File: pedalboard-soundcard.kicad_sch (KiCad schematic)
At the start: 21 parts, among them J1 RPi_GPIO, U1 AT24CS01-STUM, U2 NCP163, U3 NCP163, U5 NCP163

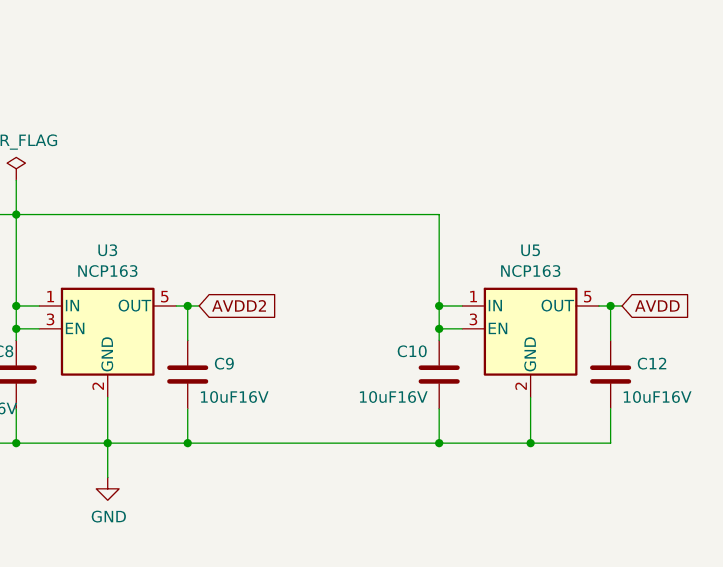
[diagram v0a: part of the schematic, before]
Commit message: Use Power Symbols for analog power
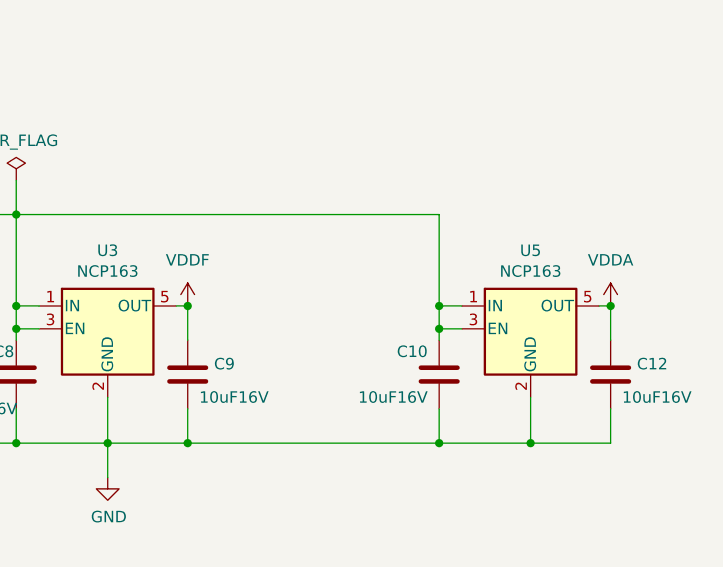
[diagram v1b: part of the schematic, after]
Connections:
- net AVDD renamed VDDA
- net AVDD2 renamed VDDF

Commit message: Add Fiducials and OSHW logo
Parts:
- added FID1, FID2, FID3, FID4: Fiducial, Fiducial:Fiducial_0.75mm_Mask1.5mm, symbol Mechanical:Fiducial
- added SYM1: Logo_Open_Hardware_Small, Symbol:OSHW-Logo2_9.8x8mm_SilkScreen, symbol Graphic:Logo_Open_Hardware_Small
- H1, H2, H3, H4: now left out of the parts list
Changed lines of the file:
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@@
   )
   (symbol (lib_id "Mechanical:MountingHole") (at 26.67 180.34 0) (unit 1)
-    (in_bom yes) (on_board yes) (dnp no) (fields_autoplaced)
+    (in_bom no) (on_board yes) (dnp no) (fields_autoplaced)
     (property "Reference" "H1" (at 29.21 179.07 0)
       (effects (font (size 1.27 1.27)) (justify left))
@@
   )
   (symbol (lib_id "Mechanical:MountingHole") (at 45.72 189.23 0) (unit 1)
-    (in_bom yes) (on_board yes) (dnp no) (fields_autoplaced)
+    (in_bom no) (on_board yes) (dnp no) (fields_autoplaced)
     (property "Reference" "H4" (at 48.26 187.96 0)
       (effects (font (size 1.27 1.27)) (justify left))
@@
   )
   (symbol (lib_id "Mechanical:MountingHole") (at 45.72 180.34 0) (unit 1)
-    (in_bom yes) (on_board yes) (dnp no) (fields_autoplaced)
+    (in_bom no) (on_board yes) (dnp no) (fields_autoplaced)
     (property "Reference" "H3" (at 48.26 179.07 0)
       (effects (font (size 1.27 1.27)) (justify left))
@@
         (path "/684ba6b6-4674-4c20-b126-c7deb678f8f5"
           (reference "C8") (unit 1)
+        )
+      )
+    )
+  )
+  (symbol (lib_id "Graphic:Logo_Open_Hardware_Small") (at 29.21 161.29 0) (unit 1)
+    (in_bom no) (on_board yes) (dnp no) (fields_autoplaced)
+    (property "Reference" "SYM1" (at 29.21 154.305 0)
+      (effects (font (size 1.27 1.27)) hide)
+    )
+    (property "Value" "Logo_Open_Hardware_Small" (at 29.21 167.005 0)
+      (effects (font (size 1.27 1.27)) hide)
+    )
+    (property "Footprint" "Symbol:OSHW-Logo2_9.8x8mm_SilkScreen" (at 29.21 161.29 0)
+      (effects (font (size 1.27 1.27)) hide)
+    )
+    (property "Datasheet" "~" (at 29.21 161.29 0)
+      (effects (font (size 1.27 1.27)) hide)
+    )
+    (property "Sim.Enable" "0" (at 29.21 161.29 0)
+      (effects (font (size 1.27 1.27)) hide)
+    )
+    (instances
+      (project "pedalboard-soundcard"
+        (path "/257597c6-fbef-4478-b0f4-968f2d6f1866"
+          (reference "SYM1") (unit 1)
         )
       )
@@
     )
   )
+  (symbol (lib_id "Mechanical:Fiducial") (at 80.01 179.07 0) (unit 1)
+    (in_bom no) (on_board yes) (dnp no) (fields_autoplaced)
+    (property "Reference" "FID1" (at 82.55 177.8 0)
+      (effects (font (size 1.27 1.27)) (justify left))
+    )
+    (property "Value" "Fiducial" (at 82.55 180.34 0)
+      (effects (font (size 1.27 1.27)) (justify left))
+    )
+    (property "Footprint" "Fiducial:Fiducial_0.75mm_Mask1.5mm" (at 80.01 179.07 0)
+      (effects (font (size 1.27 1.27)) hide)
+    )
+    (property "Datasheet" "~" (at 80.01 179.07 0)
+      (effects (font (size 1.27 1.27)) hide)
+    )
+    (property "Sim.Enable" "0" (at 80.01 179.07 0)
+      (effects (font (size 1.27 1.27)) hide)
+    )
+    (instances
+      (project "pedalboard-soundcard"
+        (path "/257597c6-fbef-4478-b0f4-968f2d6f1866"
+          (reference "FID1") (unit 1)
+        )
+      )
+    )
+  )
   (symbol (lib_id "power:GND") (at 77.47 83.82 0) (unit 1)
     (in_bom yes) (on_board yes) (dnp no) (fields_autoplaced)
@@
   )
   (symbol (lib_id "Mechanical:MountingHole") (at 26.67 189.23 0) (unit 1)
-    (in_bom yes) (on_board yes) (dnp no) (fields_autoplaced)
+    (in_bom no) (on_board yes) (dnp no) (fields_autoplaced)
     (property "Reference" "H2" (at 29.21 187.96 0)
       (effects (font (size 1.27 1.27)) (justify left))
@@
         (path "/257597c6-fbef-4478-b0f4-968f2d6f1866"
           (reference "#PWR037") (unit 1)
+        )
+      )
+    )
+  )
+  (symbol (lib_id "Mechanical:Fiducial") (at 80.01 190.5 0) (unit 1)
+    (in_bom no) (on_board yes) (dnp no) (fields_autoplaced)
+    (property "Reference" "FID3" (at 82.55 189.23 0)
+      (effects (font (size 1.27 1.27)) (justify left))
+    )
+    (property "Value" "Fiducial" (at 82.55 191.77 0)
+      (effects (font (size 1.27 1.27)) (justify left))
+    )
+    (property "Footprint" "Fiducial:Fiducial_0.75mm_Mask1.5mm" (at 80.01 190.5 0)
+      (effects (font (size 1.27 1.27)) hide)
+    )
+    (property "Datasheet" "~" (at 80.01 190.5 0)
+      (effects (font (size 1.27 1.27)) hide)
+    )
+    (property "Sim.Enable" "0" (at 80.01 190.5 0)
+      (effects (font (size 1.27 1.27)) hide)
+    )
+    (instances
+      (project "pedalboard-soundcard"
+        (path "/257597c6-fbef-4478-b0f4-968f2d6f1866"
+          (reference "FID3") (unit 1)
+        )
+      )
+    )
+  )
+  (symbol (lib_id "Mechanical:Fiducial") (at 102.87 190.5 0) (unit 1)
+    (in_bom no) (on_board yes) (dnp no) (fields_autoplaced)
+    (property "Reference" "FID4" (at 105.41 189.23 0)
+      (effects (font (size 1.27 1.27)) (justify left))
+    )
+    (property "Value" "Fiducial" (at 105.41 191.77 0)
+      (effects (font (size 1.27 1.27)) (justify left))
+    )
+    (property "Footprint" "Fiducial:Fiducial_0.75mm_Mask1.5mm" (at 102.87 190.5 0)
+      (effects (font (size 1.27 1.27)) hide)
+    )
+    (property "Datasheet" "~" (at 102.87 190.5 0)
+      (effects (font (size 1.27 1.27)) hide)
+    )
+    (property "Sim.Enable" "0" (at 102.87 190.5 0)
+      (effects (font (size 1.27 1.27)) hide)
+    )
+    (instances
+      (project "pedalboard-soundcard"
+        (path "/257597c6-fbef-4478-b0f4-968f2d6f1866"
+          (reference "FID4") (unit 1)
         )
       )
@@
         )
       )
+    )
+  )
+  (symbol (lib_id "Mechanical:Fiducial") (at 102.87 179.07 0) (unit 1)
+    (in_bom no) (on_board yes) (dnp no) (fields_autoplaced)
+    (property "Reference" "FID2" (at 105.41 177.8 0)
+      (effects (font (size 1.27 1.27)) (justify left))
+    )
+    (property "Value" "Fiducial" (at 105.41 180.34 0)
+      (effects (font (size 1.27 1.27)) (justify left))
+    )
+    (property "Footprint" "Fiducial:Fiducial_0.75mm_Mask1.5mm" (at 102.87 179.07 0)
+      (effects (font (size 1.27 1.27)) hide)
+    )
+    (property "Datasheet" "~" (at 102.87 179.07 0)
+      (effects (font (size 1.27 1.27)) hide)
+    )
+    (property "Sim.Enable" "0" (at 102.87 179.07 0)
+      (effects (font (size 1.27 1.27)) hide)
+    )
+    (instances
+      (project "pedalboard-soundcard"
+        (path "/257597c6-fbef-4478-b0f4-968f2d6f1866"
+          (reference "FID2") (unit 1)
+        )
+      )

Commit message: Smaller OSHW Logo
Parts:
- SYM1: footprint Symbol:OSHW-Logo2_9.8x8mm_SilkScreen -> Symbol:OSHW-Logo_5.7x6mm_SilkScreen
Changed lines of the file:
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@@
     )
   )
-  (symbol (lib_id "Graphic:Logo_Open_Hardware_Small") (at 29.21 161.29 0) (unit 1)
+  (symbol (lib_id "Graphic:Logo_Open_Hardware_Small") (at 139.7 185.42 0) (unit 1)
     (in_bom no) (on_board yes) (dnp no) (fields_autoplaced)
-    (property "Reference" "SYM1" (at 29.21 154.305 0)
+    (property "Reference" "SYM1" (at 139.7 178.435 0)
       (effects (font (size 1.27 1.27)) hide)
     )
-    (property "Value" "Logo_Open_Hardware_Small" (at 29.21 167.005 0)
+    (property "Value" "Logo_Open_Hardware_Small" (at 139.7 191.135 0)
       (effects (font (size 1.27 1.27)) hide)
     )
-    (property "Footprint" "Symbol:OSHW-Logo2_9.8x8mm_SilkScreen" (at 29.21 161.29 0)
+    (property "Footprint" "Symbol:OSHW-Logo_5.7x6mm_SilkScreen" (at 139.7 185.42 0)
       (effects (font (size 1.27 1.27)) hide)
     )
-    (property "Datasheet" "~" (at 29.21 161.29 0)
+    (property "Datasheet" "~" (at 139.7 185.42 0)
       (effects (font (size 1.27 1.27)) hide)
     )
-    (property "Sim.Enable" "0" (at 29.21 161.29 0)
+    (property "Sim.Enable" "0" (at 139.7 185.42 0)
       (effects (font (size 1.27 1.27)) hide)
     )

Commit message: Add 3.5mm jack connectors
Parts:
- J1: Supplier (none) -> https://www.digikey.com/en/products/detail/adafruit-industr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
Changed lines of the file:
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@@
       (effects (font (size 1.524 1.524)) hide)
     )
-    (property "Datasheet" "" (at 29.21 26.67 0)
+    (property "Datasheet" "https://cdn-shop.adafruit.com/product-files/2222/00587.pdf" (at 29.21 26.67 0)
       (effects (font (size 1.524 1.524)))
     )
-    (property "Supplier" "" (at 29.21 26.67 0)
+    (property "Supplier" "https://www.digikey.com/en/products/detail/adafruit-industries-llc/2222/6238005" (at 29.21 26.67 0)
       (effects (font (size 1.27 1.27)) hide)
     )

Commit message: Add digikey shared list
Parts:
- J1: Supplier https://www.digikey.com/en/products/detail/adafruit-industr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 -> https://www.digikey.ch/en/products/detail/adafruit-industri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
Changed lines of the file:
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@@
       (effects (font (size 1.524 1.524)))
     )
-    (property "Supplier" "https://www.digikey.com/en/products/detail/adafruit-industries-llc/2222/6238005" (at 29.21 26.67 0)
+    (property "Supplier" "https://www.digikey.ch/en/products/detail/adafruit-industries-llc/2222/6238005" (at 29.21 26.67 0)
       (effects (font (size 1.27 1.27)) hide)
     )

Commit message: Add panel tabs
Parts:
- added T1, T2, T3, T4: Tab, PCM_kikit:Tab, symbol PCM_kikit:Tab
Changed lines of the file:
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@@
+    )
+  )
+  (symbol (lib_id "PCM_kikit:Tab") (at 105.41 160.02 0) (unit 1)
+    (in_bom no) (on_board yes) (dnp no) (fields_autoplaced)
+    (property "Reference" "T2" (at 110.49 158.115 0)
+      (effects (font (size 1.27 1.27)) (justify left))
+    )
+    (property "Value" "Tab" (at 110.49 160.655 0)
+      (effects (font (size 1.27 1.27)) (justify left))
+    )
+    (property "Footprint" "PCM_kikit:Tab" (at 105.41 160.02 0)
+      (effects (font (size 1.27 1.27)) hide)
+    )
+    (property "Datasheet" "" (at 105.41 160.02 0)
+      (effects (font (size 1.27 1.27)) hide)
+    )
+    (instances
+      (project "pedalboard-soundcard"
+        (path "/257597c6-fbef-4478-b0f4-968f2d6f1866"
+          (reference "T2") (unit 1)
+        )
+      )
     )
   )
@@
     )
   )
+  (symbol (lib_id "PCM_kikit:Tab") (at 105.41 165.1 0) (unit 1)
+    (in_bom no) (on_board yes) (dnp no) (fields_autoplaced)
+    (property "Reference" "T4" (at 110.49 163.195 0)
+      (effects (font (size 1.27 1.27)) (justify left))
+    )
+    (property "Value" "Tab" (at 110.49 165.735 0)
+      (effects (font (size 1.27 1.27)) (justify left))
+    )
+    (property "Footprint" "PCM_kikit:Tab" (at 105.41 165.1 0)
+      (effects (font (size 1.27 1.27)) hide)
+    )
+    (property "Datasheet" "" (at 105.41 165.1 0)
+      (effects (font (size 1.27 1.27)) hide)
+    )
+    (instances
+      (project "pedalboard-soundcard"
+        (path "/257597c6-fbef-4478-b0f4-968f2d6f1866"
+          (reference "T4") (unit 1)
+        )
+      )
+    )
+  )
   (symbol (lib_id "Device:R") (at 85.09 74.93 270) (unit 1)
     (in_bom yes) (on_board yes) (dnp no)
@@
         (path "/684ba6b6-4674-4c20-b126-c7deb678f8f5"
           (reference "C7") (unit 1)
+        )
+      )
+    )
+  )
+  (symbol (lib_id "PCM_kikit:Tab") (at 83.82 165.1 0) (unit 1)
+    (in_bom no) (on_board yes) (dnp no) (fields_autoplaced)
+    (property "Reference" "T3" (at 88.9 163.195 0)
+      (effects (font (size 1.27 1.27)) (justify left))
+    )
+    (property "Value" "Tab" (at 88.9 165.735 0)
+      (effects (font (size 1.27 1.27)) (justify left))
+    )
+    (property "Footprint" "PCM_kikit:Tab" (at 83.82 165.1 0)
+      (effects (font (size 1.27 1.27)) hide)
+    )
+    (property "Datasheet" "" (at 83.82 165.1 0)
+      (effects (font (size 1.27 1.27)) hide)
+    )
+    (instances
+      (project "pedalboard-soundcard"
+        (path "/257597c6-fbef-4478-b0f4-968f2d6f1866"
+          (reference "T3") (unit 1)
         )
       )
@@
         )
       )
+    )
+  )
+  (symbol (lib_id "PCM_kikit:Tab") (at 83.82 160.02 0) (unit 1)
+    (in_bom no) (on_board yes) (dnp no) (fields_autoplaced)
+    (property "Reference" "T1" (at 88.9 158.115 0)
+      (effects (font (size 1.27 1.27)) (justify left))
+    )
+    (property "Value" "Tab" (at 88.9 160.655 0)
+      (effects (font (size 1.27 1.27)) (justify left))
+    )
+    (property "Footprint" "PCM_kikit:Tab" (at 83.82 160.02 0)
+      (effects (font (size 1.27 1.27)) hide)
+    )
+    (property "Datasheet" "" (at 83.82 160.02 0)
+      (effects (font (size 1.27 1.27)) hide)
+    )
+    (instances
+      (project "pedalboard-soundcard"
+        (path "/257597c6-fbef-4478-b0f4-968f2d6f1866"
+          (reference "T1") (unit 1)
+        )
+      )
